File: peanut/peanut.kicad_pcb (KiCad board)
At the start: 4 copper layers, 51 x 24.5 mm, 72 parts, among them J1 USB-C, J2 PYRO_OUT, J3 Battery JST, J4 Arming, Q1 NMOS, Q2 NMOS, Q3 NMOS, Q4 NMOS, Q5 PMOS, U1 MS5611-01BA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

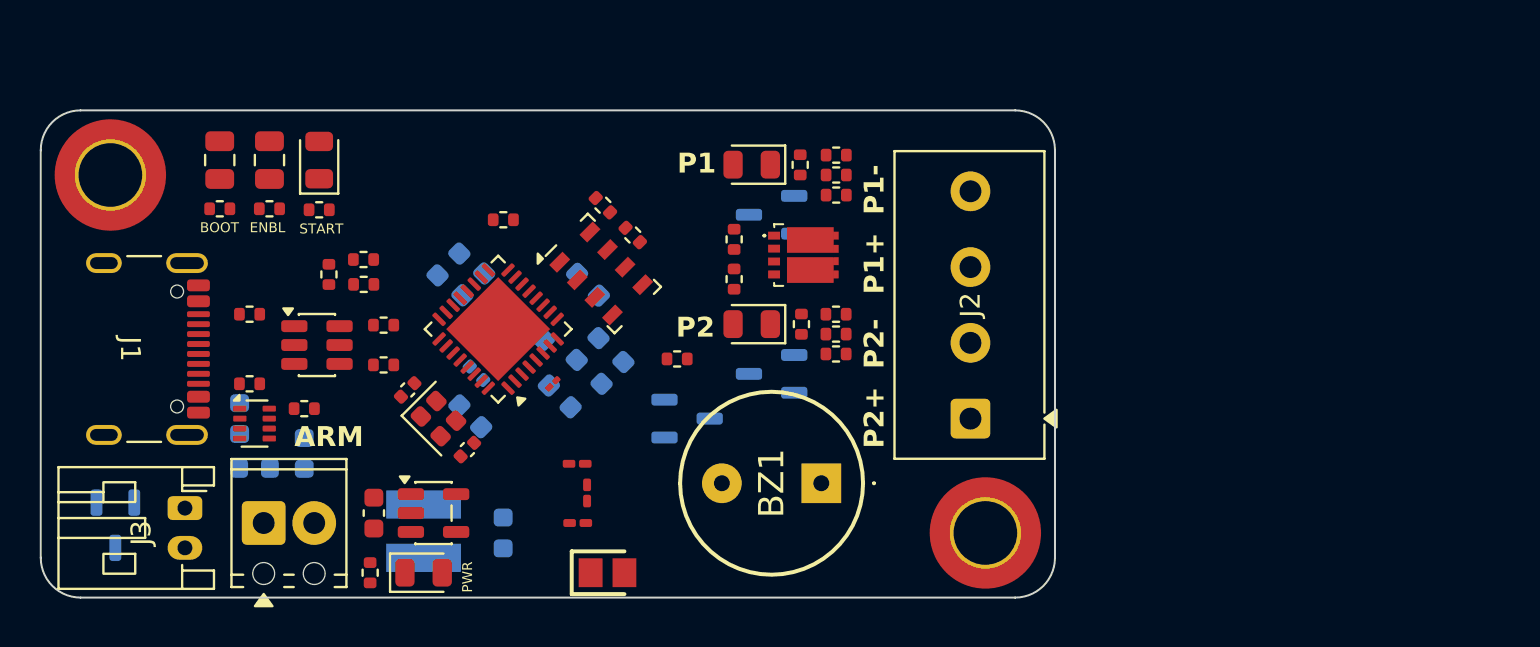
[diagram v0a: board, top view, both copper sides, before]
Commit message: feat: Shrink board
Shrinks the board length-wise more.
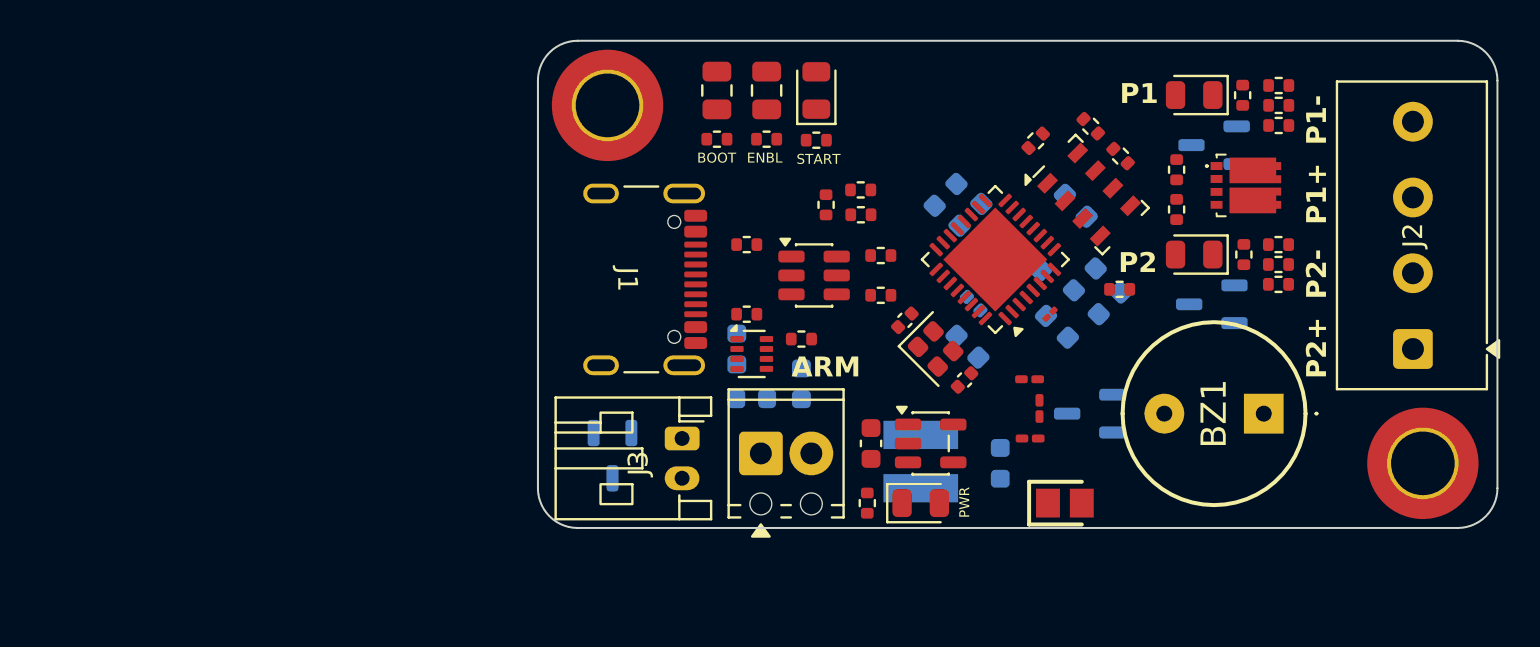
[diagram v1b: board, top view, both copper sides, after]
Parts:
- moved R8 27.1 mm to (145.0, 90.0), turned to -135 degrees
- moved J4 25.2 mm to (131.2, 105.8)
- moved R21 25.2 mm to (136.2, 92.5)
- moved R5 25.2 mm to (137.2, 95.8)
- moved R6 25.2 mm to (137.2, 97.8)
- moved C10 25.2 mm to (140.5, 92.8)
- moved C11 25.2 mm to (141.8, 93.8)
- moved C14 25.2 mm to (136.8, 105.2)
- moved C15 25.2 mm to (143.2, 106.2)
- moved C16 25.2 mm to (130.8, 103.0)
- moved C17 25.2 mm to (130.0, 100.5)
- moved C18 25.2 mm to (133.2, 102.2)
- moved C4 25.2 mm to (148.8, 98.2)
- moved C5 25.2 mm to (147.5, 97.0)
- moved C9 25.2 mm to (144.8, 96.0)
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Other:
- board size 51 x 24.5 mm -> 48.2 x 24.5 mm

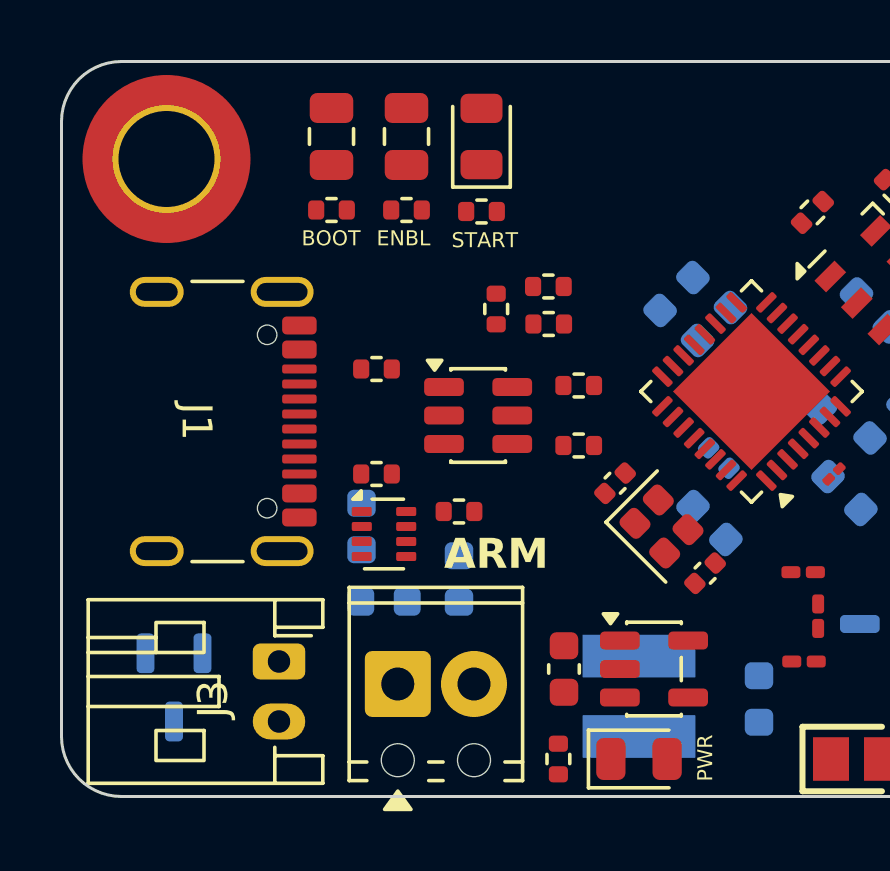
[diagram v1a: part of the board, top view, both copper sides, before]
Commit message: feat: Verify component features
Completed most of the review checklist for the initial revision. Routing
can commence once design rules are updated.
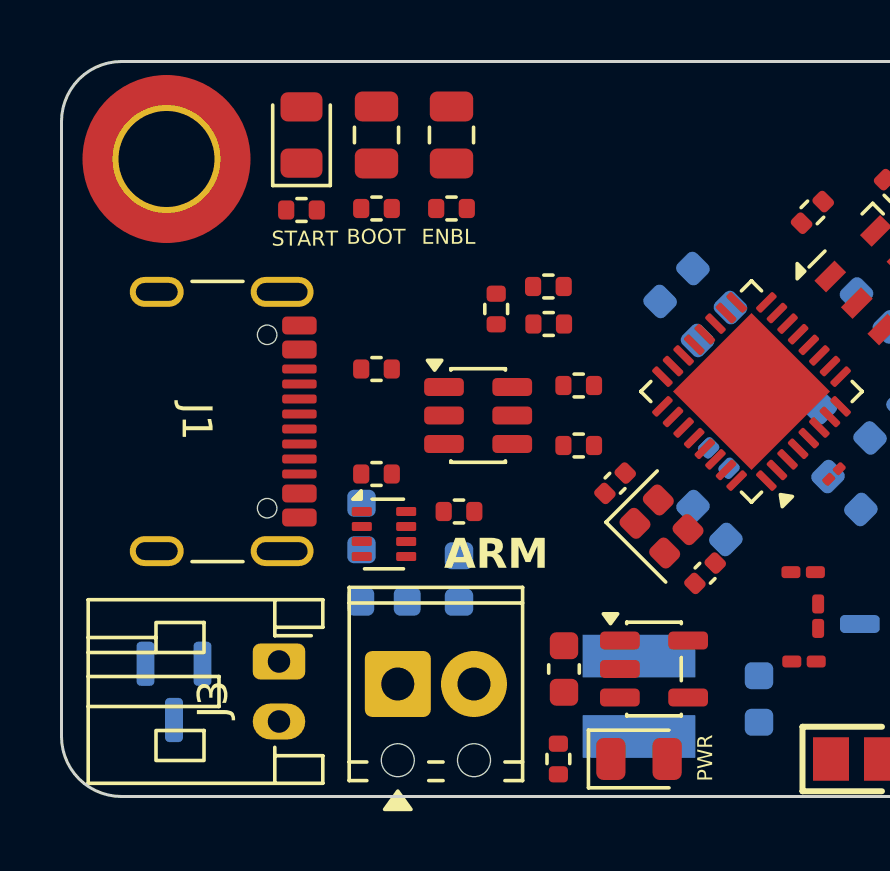
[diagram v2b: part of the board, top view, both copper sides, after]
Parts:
- Q5: footprint Package_TO_SOT_SMD:SOT-23-3 -> Package_TO_SOT_SMD:SOT-23
- R25, R26: value 2k2 -> 10k
- Y1: value 40MHz -> 40MHz +/-10ppm
- moved D1 6.00 mm to (128.0, 87.4)
- moved R7 6.00 mm to (128.0, 89.9)
- moved R1 1.50 mm to (133.0, 89.9)
- moved R2 1.50 mm to (130.5, 89.9)
- moved JP1 1.50 mm to (133.0, 87.4)
- moved JP2 1.50 mm to (130.5, 87.4)
- moved C10 0.30 mm to (140.5, 92.4)
- moved Q5 0.15 mm to (123.8, 106.0)
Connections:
- J1 pad SH: (no net) -> GND
- J2 pad 1: VBAT -> VBAT_RAW
- J2 pad 3: VBAT -> VBAT_RAW
- J3 pad 2: /Power/BAT+ -> VBAT_RAW
- Q5 pad 3: /Power/BAT+ -> VBAT_RAW

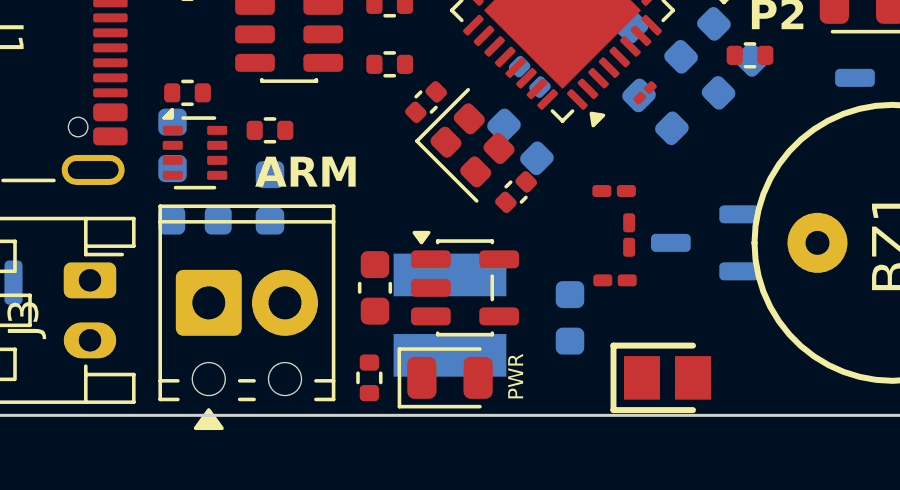
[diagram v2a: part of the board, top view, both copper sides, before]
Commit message: feat: Cheaper inductor
Swapped inductor for one that is cheaper. Current board cost (minus JST
connector since that is not available on Mouser) is $44.76 CAD in
components.
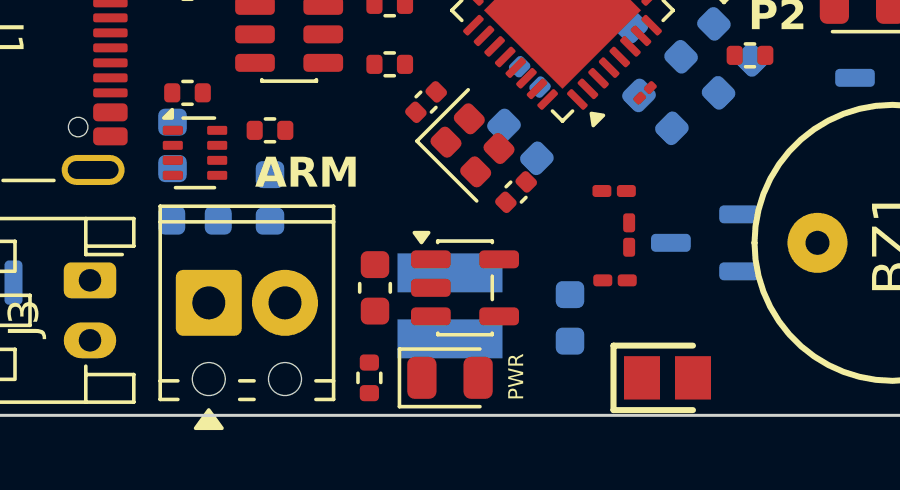
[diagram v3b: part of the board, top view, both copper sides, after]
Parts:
- L3: footprint LPO3310-222MLC:LPO3310222MLC -> SRN3015BTA-2R2M:SRN3015BTA2R2M
- moved L3 0.31 mm to (139.2, 105.8)
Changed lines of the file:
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@@
 			)
 		)
-		(property "MPN" "SFR01MZPJ103"
+		(property "MPN" "MCS04020C1002FE000"
 			(at 0 0 225)
 			(unlocked yes)
@@
 			)
 		)
-		(property "MPN" "SFR01MZPJ103"
+		(property "MPN" "MCS04020C1002FE000"
 			(at 0 0 270)
 			(unlocked yes)
@@
 			)
 		)
-		(property "MPN" "SFR01MZPJ103"
+		(property "MPN" "MCS04020C1002FE000"
 			(at 0 0 0)
 			(unlocked yes)
@@
 			)
 		)
-		(property "MPN" "SFR01MZPJ103"
+		(property "MPN" "MCS04020C1002FE000"
 			(at 0 0 180)
 			(unlocked yes)
@@
 			)
 		)
-		(property "MPN" "SFR01MZPJ103"
+		(property "MPN" "MCS04020C1002FE000"
 			(at 0 0 0)
 			(unlocked yes)
@@
 			)
 		)
-		(property "MPN" "SFR01MZPJ103"
+		(property "MPN" "MCS04020C1002FE000"
 			(at 0 0 180)
 			(unlocked yes)
@@
 			)
 		)
-		(property "MPN" "-"
+		(property "MPN" ""
 			(at 0 0 90)
 			(unlocked yes)
@@
 			)
 		)
-		(property "MPN" "SFR01MZPJ103"
+		(property "MPN" "MCS04020C1002FE000"
 			(at 0 0 315)
 			(unlocked yes)
@@
 			)
 		)
-		(property "MPN" "SFR01MZPJ103"
+		(property "MPN" "MCS04020C1002FE000"
 			(at 0 0 0)
 			(unlocked yes)
@@
 			)
 		)
-		(property "MPN" "SFR01MZPJ103"
+		(property "MPN" "MCS04020C1002FE000"
 			(at 0 0 180)
 			(unlocked yes)
@@
 			)
 		)
-		(property "MPN" "SFR01MZPJ103"
+		(property "MPN" "MCS04020C1002FE000"
 			(at 0 0 180)
 			(unlocked yes)
@@
 			)
 		)
-		(property "MPN" "LM3671MF-3.3/NOPB"
+		(property "MPN" "LM3671MFX-3.3/NOPB"
 			(at 0 0 0)
 			(unlocked yes)
@@
 			)
 		)
-		(property "MPN" "-"
+		(property "MPN" ""
 			(at 0 0 90)
 			(unlocked yes)
@@
 			)
 		)
-		(property "MPN" "SFR01MZPJ103"
+		(property "MPN" "MCS04020C1002FE000"
 			(at 0 0 90)
 			(unlocked yes)
@@
 			)
 		)
-		(property "MPN" "SFR01MZPJ103"
+		(property "MPN" "MCS04020C1002FE000"
 			(at 0 0 135)
 			(unlocked yes)
@@
 		)
 	)
-	(footprint "LPO3310-222MLC:LPO3310222MLC"
+	(footprint "SRN3015BTA-2R2M:SRN3015BTA2R2M"
 		(layer "B.Cu")
-		(at 139.25 106.16 -90)
-		(descr "3.3x3.3x1.0mm")
+		(at 139.25 105.849999 -90)
+		(descr "SRN3015BTA-2R2M")
 		(tags "Inductor")
 		(property "Reference" "L3"
 			(at 0 0 90)
 			(layer "B.SilkS")
-			(hide yes)
 			(effects
 				(font
@@
 			)
 		)
-		(property "Datasheet" "https://www.mouser.ca/datasheet/3/995/1/lpo3310.pdf"
+		(property "Datasheet" "https://www.mouser.com/catalog/specsheets/Bourns_08042023_SRN3015BTA_datasheet.pdf"
 			(at 0 0 90)
 			(layer "B.Fab")
@@
 			)
 		)
-		(property "MPN" "LPO3310-222MLC"
-			(at 0 0 90)
+		(property "MPN" "SRN3015BTA-2R2M"
+			(at 0 0 270)
 			(unlocked yes)
 			(layer "B.Fab")
@@
 		(sheetname "/Power/")
 		(sheetfile "power.kicad_sch")
-		(units
-			(unit
-				(name "A")
-				(pins "1" "2")
-			)
-		)
 		(attr smd)
 		(duplicate_pad_numbers_are_jumpers no)
 		(fp_line
-			(start -0.2 1.65)
-			(end 0.2 1.65)
+			(start -0.2 1.5)
+			(end 0.2 1.5)
 			(stroke
 				(width 0.2)
@@
 		)
 		(fp_line
-			(start -2.600001 0)
-			(end -2.600001 0)
+			(start -2.3 0)
+			(end -2.3 0)
 			(stroke
 				(width 0.1)
@@
 		)
 		(fp_line
-			(start -2.5 0)
-			(end -2.5 0)
+			(start -2.2 0)
+			(end -2.2 0)
 			(stroke
 				(width 0.1)
@@
 		)
 		(fp_line
-			(start -0.2 -1.65)
-			(end 0.2 -1.65)
+			(start -0.2 -1.5)
+			(end 0.2 -1.5)
 			(stroke
 				(width 0.2)
@@
 		)
 		(fp_arc
-			(start -2.600001 0)
-			(mid -2.55 -0.050001)
-			(end -2.5 0)
+			(start -2.3 0)
+			(mid -2.25 -0.05)
+			(end -2.2 0)
 			(stroke
 				(width 0.1)
@@
 		)
 		(fp_arc
-			(start -2.5 0)
-			(mid -2.55 0.05)
-			(end -2.600001 0)
+			(start -2.2 0)
+			(mid -2.25 0.05)
+			(end -2.3 0)
 			(stroke
 				(width 0.1)
@@
 		)
 		(fp_line
-			(start -3.05 2.88)
-			(end 3.05 2.88)
+			(start -2.75 2.75)
+			(end 2.75 2.75)
 			(stroke
 				(width 0.1)
@@
 		)
 		(fp_line
-			(start 3.05 2.88)
-			(end 3.05 -2.88)
+			(start 2.75 2.75)
+			(end 2.75 -2.75)
 			(stroke
 				(width 0.1)
@@
 		)
 		(fp_line
-			(start -3.05 -2.88)
-			(end -3.05 2.88)
+			(start -2.75 -2.75)
+			(end -2.75 2.75)
 			(stroke
 				(width 0.1)
@@
 		)
 		(fp_line
-			(start 3.05 -2.88)
-			(end -3.05 -2.88)
+			(start 2.75 -2.75)
+			(end -2.75 -2.75)
 			(stroke
 				(width 0.1)
@@
 		)
 		(fp_line
-			(start -1.65 1.65)
-			(end 1.65 1.65)
+			(start -1.5 1.5)
+			(end -1.5 -1.5)
 			(stroke
 				(width 0.1)
@@
 		)
 		(fp_line
-			(start 1.65 1.65)
-			(end 1.65 -1.65)
+			(start 1.5 1.5)
+			(end -1.5 1.5)
 			(stroke
 				(width 0.1)
@@
 		)
 		(fp_line
-			(start -1.65 -1.65)
-			(end -1.65 1.65)
+			(start -1.5 -1.5)
+			(end 1.5 -1.5)
 			(stroke
 				(width 0.1)
@@
 		)
 		(fp_line
-			(start 1.65 -1.65)
-			(end -1.65 -1.65)
+			(start 1.5 -1.5)
+			(end 1.5 1.5)
 			(stroke
 				(width 0.1)
@@
 		)
 		(pad "1" smd rect
-			(at -1.34 0 270)
-			(size 1.42 3.76)
+			(at -1.1 0 270)
+			(size 1.3 3.5)
 			(layers "B.Cu" "B.Mask" "B.Paste")
 			(net "Net-(U4-SW)")
@@
 		)
 		(pad "2" smd rect
-			(at 1.34 0 270)
-			(size 1.42 3.76)
+			(at 1.1 0 270)
+			(size 1.3 3.5)
 			(layers "B.Cu" "B.Mask" "B.Paste")
 			(net "3V3")
@@
 		)
 		(embedded_fonts no)
+		(model "${KIPRJMOD}/../LIB_SRN3015BTA-2R2M/3D/SRN3015BTA-2R2M.stp"
+			(offset
+				(xyz 0 -0.02999999888 0.759999979)
+			)
+			(scale
+				(xyz 1 1 1)
+			)
+			(rotate
+				(xyz -180 0 90)
+			)
+		)
 	)
 	(footprint "Package_TO_SOT_SMD:SOT-23-3"

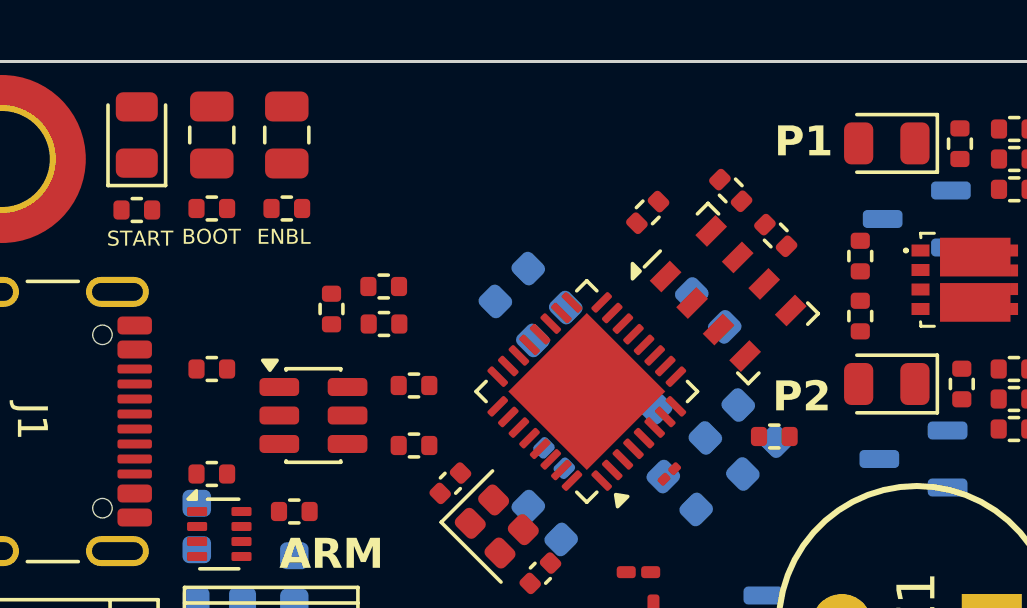
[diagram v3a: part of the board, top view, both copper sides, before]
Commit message: feat: Solder jumpers instead of capacitor footprint
The boot and enable jumpers are now solder jumpers instead of capacitors
footprints, which should make them easier to jump.
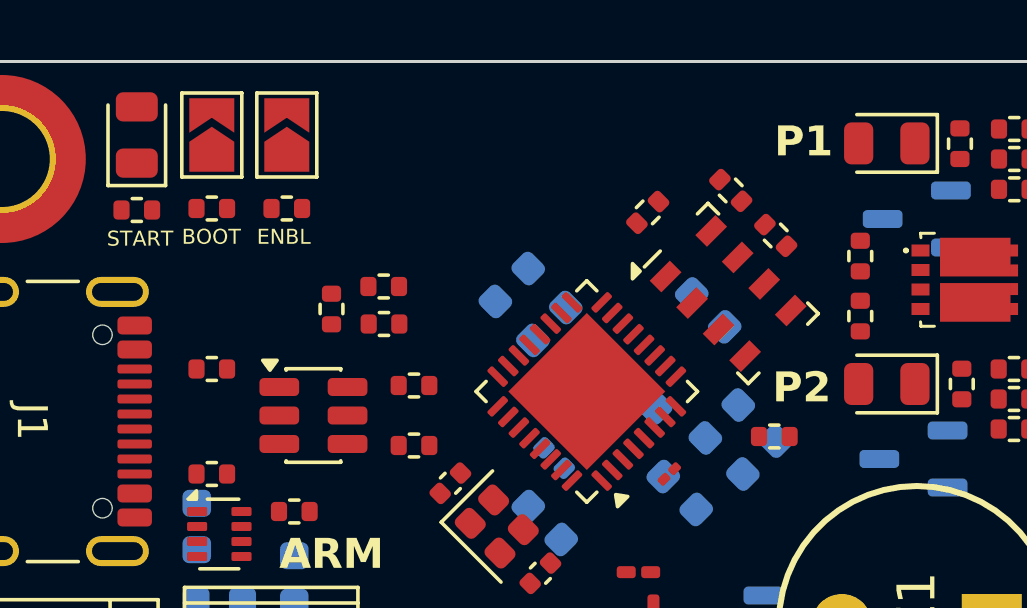
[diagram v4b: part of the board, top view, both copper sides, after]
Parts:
- JP1, JP2: footprint Capacitor_SMD:C_0805_2012Metric -> Jumper:SolderJumper-2_P1.3mm_Open_TrianglePad1.0x1.5mm

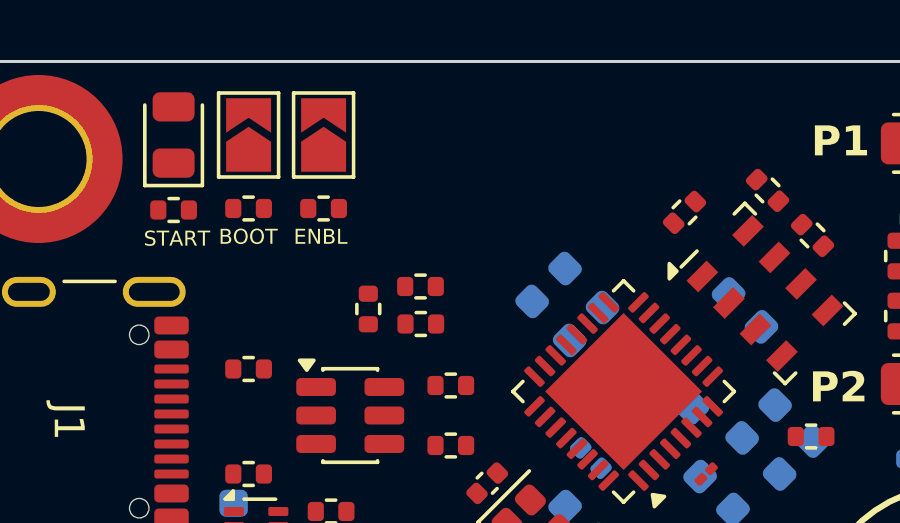
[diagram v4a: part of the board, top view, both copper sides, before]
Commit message: feat: Add silkscreen logo
Adds a board logo and my logo to the board silkscreen.
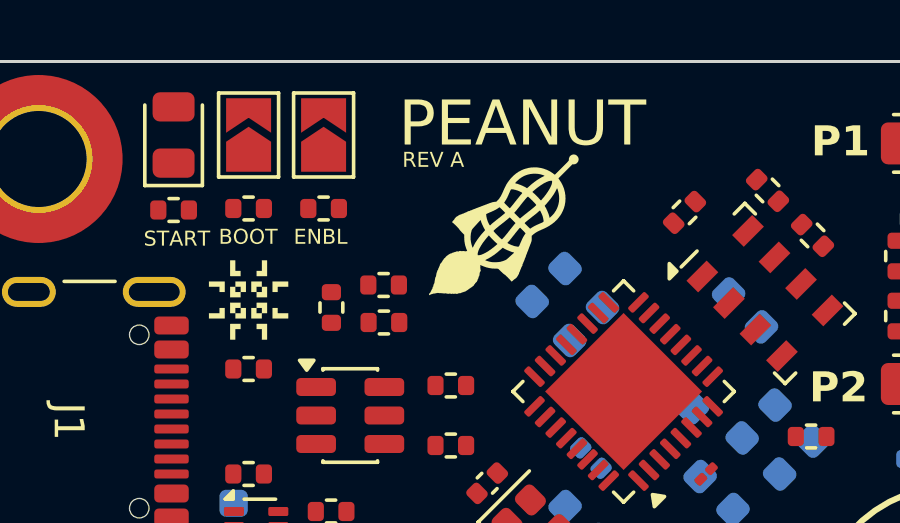
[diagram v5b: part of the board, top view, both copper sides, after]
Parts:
- added G***: LOGO, logo:Peanut-Logo_5x4.7mm_SilkScreen, F.Cu at (139.0, 90.4)
- added G***: LOGO, logo:Pulsar-Logo_3x3mm_SilkScreen, F.Cu at (130.5, 92.9)
- moved R20 1.23 mm to (135.0, 93.7)
- moved R21 1.23 mm to (135.0, 92.4)
- moved R22 1.23 mm to (133.3, 93.2)
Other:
- board text added: "PEANUT"
- board text added: "REV A"
